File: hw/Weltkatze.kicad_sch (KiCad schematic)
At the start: 19 parts, among them J1 USB_C_Receptacle_USB2.0_14P, SW1 BOOT_SEL, U1 ESP32-C3-WROOM-02

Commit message: blep
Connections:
- net ESP_DM renamed ESP_DN
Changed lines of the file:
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@@
 	(wire
 		(pts
-			(xy 207.01 71.12) (xy 207.01 60.96)
+			(xy 207.01 63.5) (xy 207.01 60.96)
 		)
 		(stroke
@@
 	(wire
 		(pts
-			(xy 204.47 68.58) (xy 204.47 60.96)
+			(xy 204.47 69.85) (xy 204.47 60.96)
 		)
 		(stroke
@@
 	(wire
 		(pts
-			(xy 256.54 38.1) (xy 257.81 38.1)
+			(xy 255.27 38.1) (xy 257.81 38.1)
 		)
 		(stroke
@@
 		(pts
 			(xy 138.43 177.8) (xy 138.43 179.07)
-		)
-		(stroke
-			(width 0)
-			(type default)
-		)
-	)
-	(wire
-		(pts
-			(xy 203.2 68.58) (xy 204.47 68.58)
 		)
 		(stroke
@@
 		)
 	)
-	(global_label "ESP_DM"
+	(global_label "ESP_DN"
 		(shape input)
 		(at 255.27 43.18 180)
@@
 		)
 		(property "Intersheetrefs" "${INTERSHEET_REFS}"
-			(at 244.9673 43.18 0)
+			(at 245.0882 43.18 0)
 			(effects
 				(font
@@
 	(global_label "ESP_DP"
 		(shape input)
-		(at 256.54 38.1 180)
-		(fields_autoplaced yes)
-		(effects
-			(font
-				(size 1.27 1.27)
-			)
-			(justify right)
-		)
-		(property "Intersheetrefs" "${INTERSHEET_REFS}"
-			(at 246.4187 38.1 0)
+		(at 255.27 38.1 180)
+		(fields_autoplaced yes)
+		(effects
+			(font
+				(size 1.27 1.27)
+			)
+			(justify right)
+		)
+		(property "Intersheetrefs" "${INTERSHEET_REFS}"
+			(at 245.1487 38.1 0)
 			(effects
 				(font
@@
 		)
 	)
-	(global_label "ESP_DM"
-		(shape input)
-		(at 203.2 68.58 270)
-		(fields_autoplaced yes)
-		(effects
-			(font
-				(size 1.27 1.27)
-			)
-			(justify right)
-		)
-		(property "Intersheetrefs" "${INTERSHEET_REFS}"
-			(at 203.2 78.8827 90)
+	(global_label "ESP_DN"
+		(shape input)
+		(at 204.47 69.85 270)
+		(fields_autoplaced yes)
+		(effects
+			(font
+				(size 1.27 1.27)
+			)
+			(justify right)
+		)
+		(property "Intersheetrefs" "${INTERSHEET_REFS}"
+			(at 204.47 80.0318 90)
 			(effects
 				(font
@@
 	(global_label "ESP_DP"
 		(shape input)
-		(at 207.01 71.12 270)
-		(fields_autoplaced yes)
-		(effects
-			(font
-				(size 1.27 1.27)
-			)
-			(justify right)
-		)
-		(property "Intersheetrefs" "${INTERSHEET_REFS}"
-			(at 207.01 81.2413 90)
-			(effects
-				(font
+		(at 207.01 63.5 270)
+		(fields_autoplaced yes)
+		(effects
+			(font
+				(size 1.27 1.27)
+			)
+			(justify right)
+		)
+		(property "Intersheetrefs" "${INTERSHEET_REFS}"
+			(at 207.01 73.6213 90)
+			(effects
+				(font

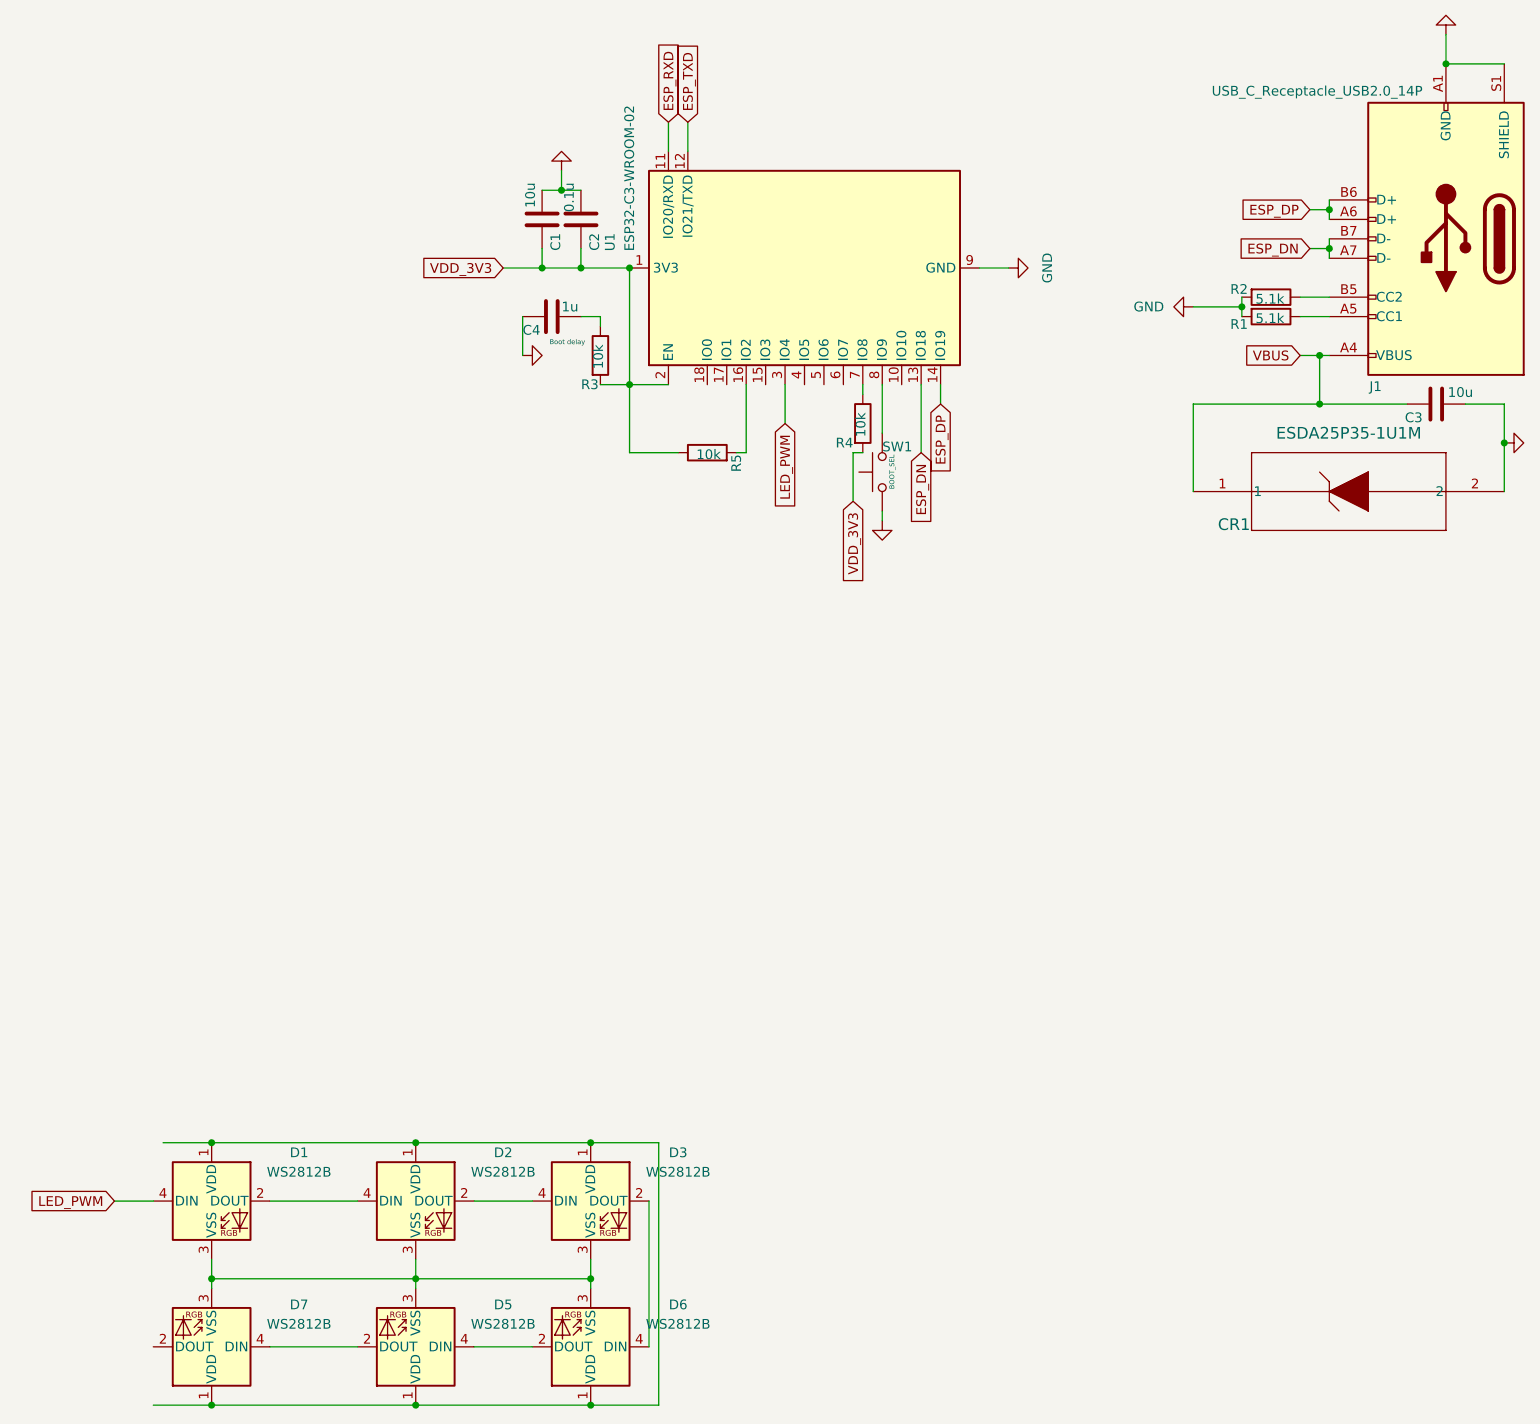
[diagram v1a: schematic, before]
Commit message: Start actual work
I've settled on the ESP32C6, as the SEEED Xiao board based on this chipset works great. So I've started work on implementing that
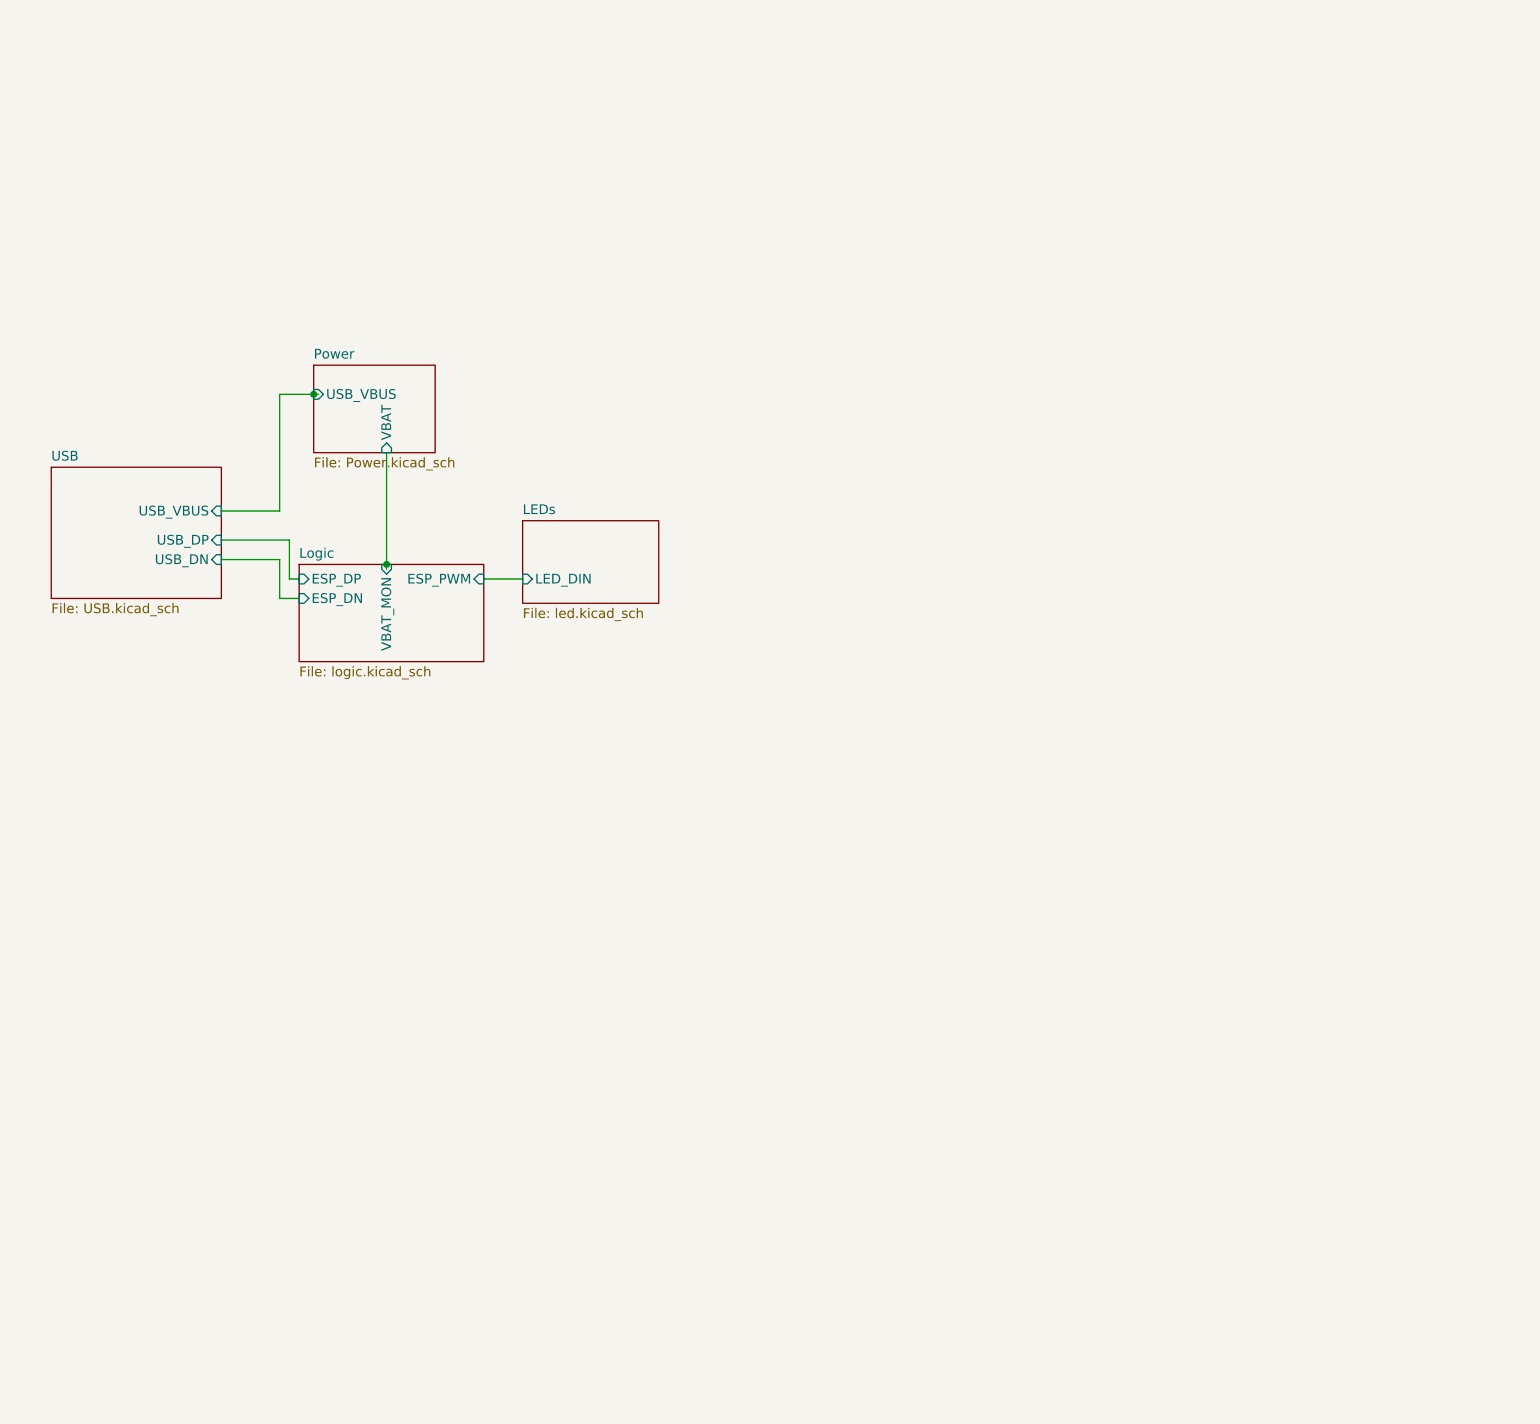
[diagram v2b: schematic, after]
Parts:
- removed C1, C3: 10u, symbol Device:C
- removed C2: 0.1u, symbol Device:C
- removed C4: 1u, symbol Device:C
- removed CR1: ESDA25P35-1U1M, QFN1610_STM, symbol ESDA25P35:ESDA25P35-1U1M
- removed D1, D2, D3, D5, D6, D7: WS2812B, LED_SMD:LED_WS2812B_PLCC4_5.0x5.0mm_P3.2mm, symbol LED:WS2812B
- removed J1: USB_C_Receptacle_USB2.0_14P, symbol Connector:USB_C_Receptacle_USB2.0_14P
- removed R1, R2: 5.1k, symbol Device:R
- removed R3, R4, R5: 10k, symbol Device:R
- removed SW1: BOOT_SEL, symbol Switch:SW_Push
- removed U1: ESP32-C3-WROOM-02, RF_Module:ESP32-C3-WROOM-02, symbol RF_Module:ESP32-C3-WROOM-02
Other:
- added sheet LEDs (led.kicad_sch)
- added sheet Logic (logic.kicad_sch)
- added sheet Power (Power.kicad_sch)
- added sheet USB (USB.kicad_sch)
- note removed: "Boot delay"

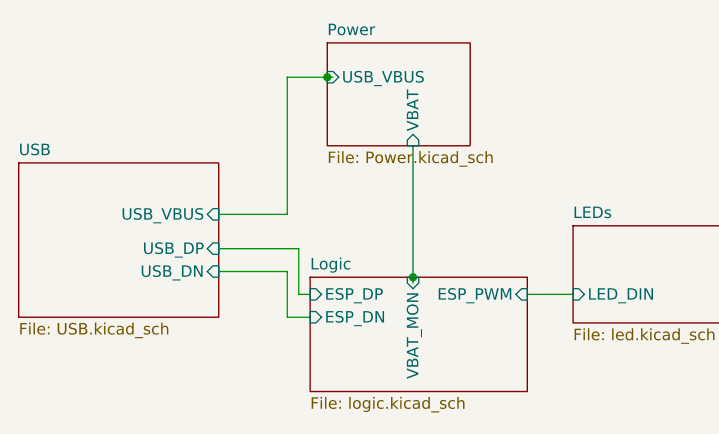
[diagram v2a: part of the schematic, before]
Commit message: Finish power stage, work on other stages
Power stage should be finalised, I've updated LED stage to include a solder jumper, to allow up to half of the LEDs to be removed in the case of power/cost savings
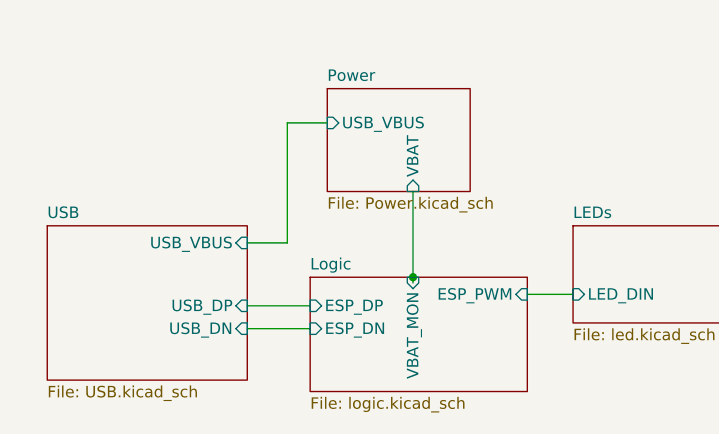
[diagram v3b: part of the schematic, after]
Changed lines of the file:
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@@
 		(color 0 0 0 0)
 	)
-	(junction
-		(at 125.095 62.23)
-		(diameter 0)
-		(color 0 0 0 0)
-	)
-	(wire
-		(pts
-			(xy 120.65 62.23) (xy 125.095 62.23)
-		)
-		(stroke
-			(width 0)
-			(type default)
-		)
-	)
-	(wire
-		(pts
-			(xy 113.03 77.47) (xy 120.65 77.47)
-		)
-		(stroke
-			(width 0)
-			(type default)
-		)
-	)
-	(wire
-		(pts
-			(xy 120.65 88.9) (xy 123.19 88.9)
-		)
-		(stroke
-			(width 0)
-			(type default)
-		)
-	)
-	(wire
-		(pts
-			(xy 113.03 83.82) (xy 120.65 83.82)
-		)
-		(stroke
-			(width 0)
-			(type default)
-		)
-	)
-	(wire
-		(pts
-			(xy 120.65 83.82) (xy 120.65 88.9)
-		)
-		(stroke
-			(width 0)
-			(type default)
-		)
-	)
-	(wire
-		(pts
-			(xy 134.62 69.85) (xy 134.62 84.455)
-		)
-		(stroke
-			(width 0)
-			(type default)
-		)
-	)
-	(wire
-		(pts
-			(xy 120.65 77.47) (xy 120.65 62.23)
-		)
-		(stroke
-			(width 0)
-			(type default)
-		)
-	)
-	(wire
-		(pts
-			(xy 125.095 62.23) (xy 125.73 62.23)
-		)
-		(stroke
-			(width 0)
-			(type default)
-		)
-	)
-	(wire
-		(pts
-			(xy 113.03 81.28) (xy 121.92 81.28)
-		)
-		(stroke
-			(width 0)
-			(type default)
-		)
-	)
-	(wire
-		(pts
-			(xy 121.92 81.28) (xy 121.92 86.36)
+	(wire
+		(pts
+			(xy 120.65 67.31) (xy 125.095 67.31)
+		)
+		(stroke
+			(width 0)
+			(type default)
+		)
+	)
+	(wire
+		(pts
+			(xy 116.205 80.645) (xy 120.65 80.645)
+		)
+		(stroke
+			(width 0)
+			(type default)
+		)
+	)
+	(wire
+		(pts
+			(xy 116.205 90.17) (xy 123.19 90.17)
+		)
+		(stroke
+			(width 0)
+			(type default)
+		)
+	)
+	(wire
+		(pts
+			(xy 134.62 74.93) (xy 134.62 84.455)
+		)
+		(stroke
+			(width 0)
+			(type default)
+		)
+	)
+	(wire
+		(pts
+			(xy 120.65 80.645) (xy 120.65 67.31)
+		)
+		(stroke
+			(width 0)
+			(type default)
+		)
+	)
+	(wire
+		(pts
+			(xy 116.205 87.63) (xy 123.19 87.63)
 		)
 		(stroke
@@
 		(pts
 			(xy 134.62 84.455) (xy 134.62 85.09)
-		)
-		(stroke
-			(width 0)
-			(type default)
-		)
-	)
-	(wire
-		(pts
-			(xy 121.92 86.36) (xy 123.19 86.36)
 		)
 		(stroke
@@
 		)
 		(pin "ESP_DP" input
-			(at 123.19 86.36 180)
+			(at 123.19 87.63 180)
 			(effects
 				(font
@@
 		)
 		(pin "ESP_DN" input
-			(at 123.19 88.9 180)
+			(at 123.19 90.17 180)
 			(effects
 				(font
@@
 	)
 	(sheet
-		(at 90.805 71.755)
+		(at 93.98 78.74)
 		(size 22.225 17.145)
 		(fields_autoplaced yes)
@@
 		)
 		(property "Sheetname" "USB"
-			(at 90.805 71.0434 0)
+			(at 93.98 78.0284 0)
 			(effects
 				(font
@@
 		)
 		(property "Sheetfile" "USB.kicad_sch"
-			(at 90.805 89.4846 0)
+			(at 93.98 96.4696 0)
 			(effects
 				(font
@@
 		)
 		(pin "USB_DP" input
-			(at 113.03 81.28 0)
+			(at 116.205 87.63 0)
 			(effects
 				(font
@@
 		)
 		(pin "USB_VBUS" input
-			(at 113.03 77.47 0)
+			(at 116.205 80.645 0)
 			(effects
 				(font
@@
 		)
 		(pin "USB_DN" input
-			(at 113.03 83.82 0)
+			(at 116.205 90.17 0)
 			(effects
 				(font
@@
 	)
 	(sheet
-		(at 125.095 58.42)
+		(at 125.095 63.5)
 		(size 15.875 11.43)
 		(fields_autoplaced yes)
@@
 		)
 		(property "Sheetname" "Power"
-			(at 125.095 57.7084 0)
+			(at 125.095 62.7884 0)
 			(effects
 				(font
@@
 		)
 		(property "Sheetfile" "Power.kicad_sch"
-			(at 125.095 70.4346 0)
+			(at 125.095 75.5146 0)
 			(effects
 				(font
@@
 		)
 		(pin "USB_VBUS" input
-			(at 125.095 62.23 180)
+			(at 125.095 67.31 180)
 			(effects
 				(font
@@
 		)
 		(pin "VBAT" input
-			(at 134.62 69.85 270)
-			(effects
-				(font
+			(at 134.62 74.93 270)
+			(effects
+				(font

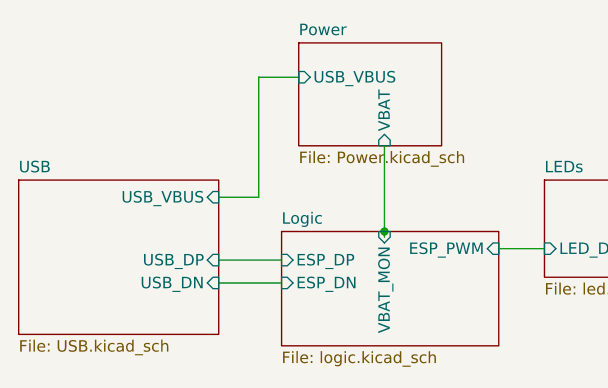
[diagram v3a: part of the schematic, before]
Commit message: Work on footprinting and PCB
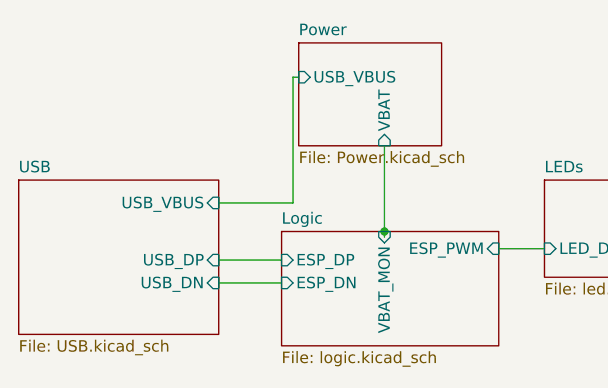
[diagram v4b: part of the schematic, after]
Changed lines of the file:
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@@
-	(wire
-		(pts
-			(xy 120.65 67.31) (xy 125.095 67.31)
-		)
-		(stroke
-			(width 0)
-			(type default)
-		)
-	)
-	(wire
-		(pts
-			(xy 116.205 80.645) (xy 120.65 80.645)
-		)
-		(stroke
-			(width 0)
-			(type default)
-		)
-	)
 	(wire
 		(pts
@@
 	(wire
 		(pts
-			(xy 120.65 80.645) (xy 120.65 67.31)
+			(xy 116.205 81.28) (xy 124.46 81.28)
 		)
 		(stroke
@@
 	(wire
 		(pts
+			(xy 124.46 67.31) (xy 125.095 67.31)
+		)
+		(stroke
+			(width 0)
+			(type default)
+		)
+	)
+	(wire
+		(pts
 			(xy 147.32 86.36) (xy 152.4 86.36)
+		)
+		(stroke
+			(width 0)
+			(type default)
+		)
+	)
+	(wire
+		(pts
+			(xy 124.46 81.28) (xy 124.46 67.31)
 		)
 		(stroke
@@
 		)
 		(pin "USB_VBUS" input
-			(at 116.205 80.645 0)
+			(at 116.205 81.28 0)
 			(effects
 				(font

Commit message: Footprinting, begin layout
I've assigned all the footprints except a few, so I've started on layout.
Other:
- title: (none) -> Weltkatze
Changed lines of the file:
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@@
 	(generator_version "8.0")
 	(paper "A4")
+	(title_block
+		(title "Weltkatze")
+		(date "2025-02-25")
+		(rev "1")
+		(comment 1 "A light up Zigbee kitty")
+	)
 	(junction
 		(at 134.62 84.455)
